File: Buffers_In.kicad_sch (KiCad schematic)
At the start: 29 parts, among them J1 NMJ6HCD2, U3 NE5532, U4 NE5532

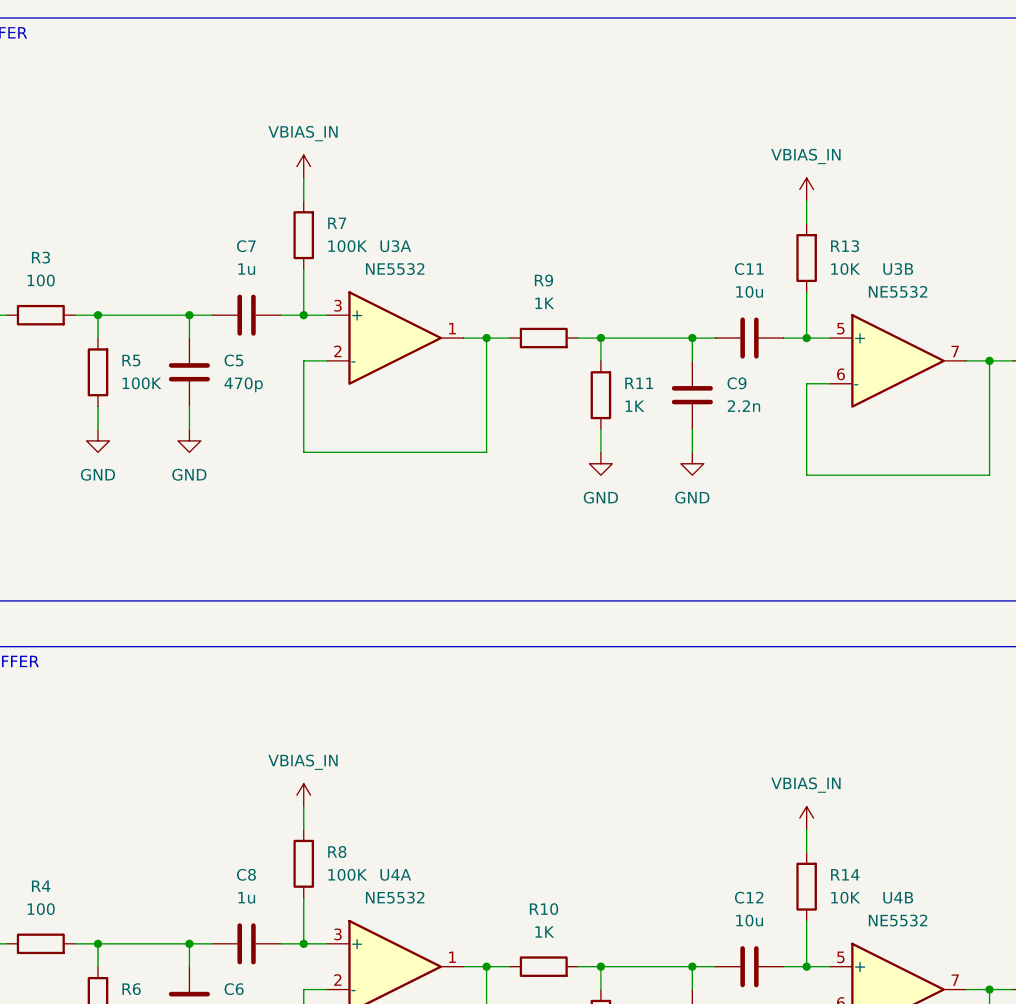
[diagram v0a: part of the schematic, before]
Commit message: Schematic
Updated the schematic.
Added the codec schematic module.
Added the buffer schematic module.
Added the RP2350 schematic module.
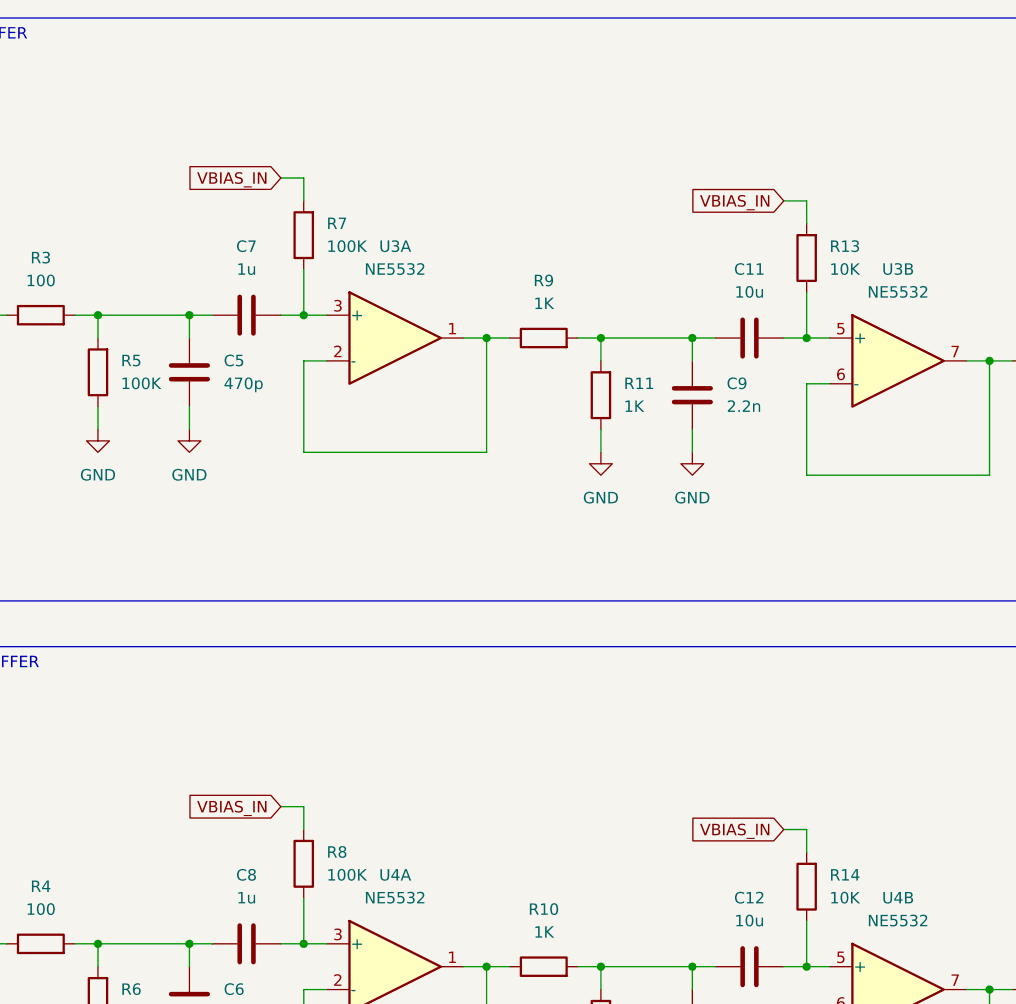
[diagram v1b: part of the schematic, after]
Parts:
- C10, C5, C6, C9: footprint (none) -> Capacitor_SMD:C_0603_1608Metric
- C11, C12, C13, C14: footprint (none) -> Capacitor_SMD:C_1206_3216Metric
- C7, C8: footprint (none) -> Capacitor_SMD:C_0805_2012Metric

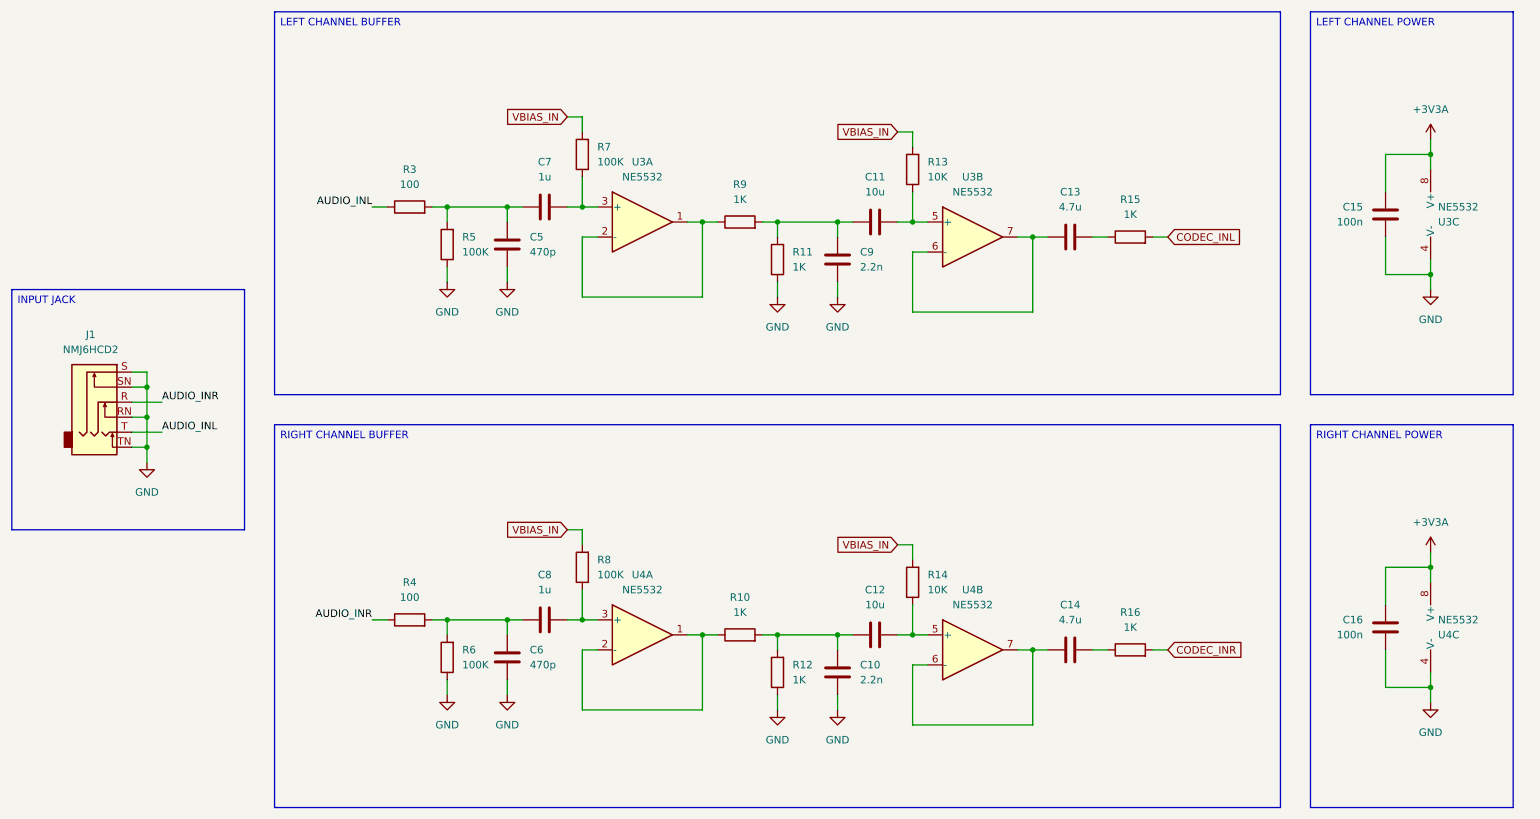
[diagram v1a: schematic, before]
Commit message: Schematic
Updated the power delivery module.
Other minor changes.
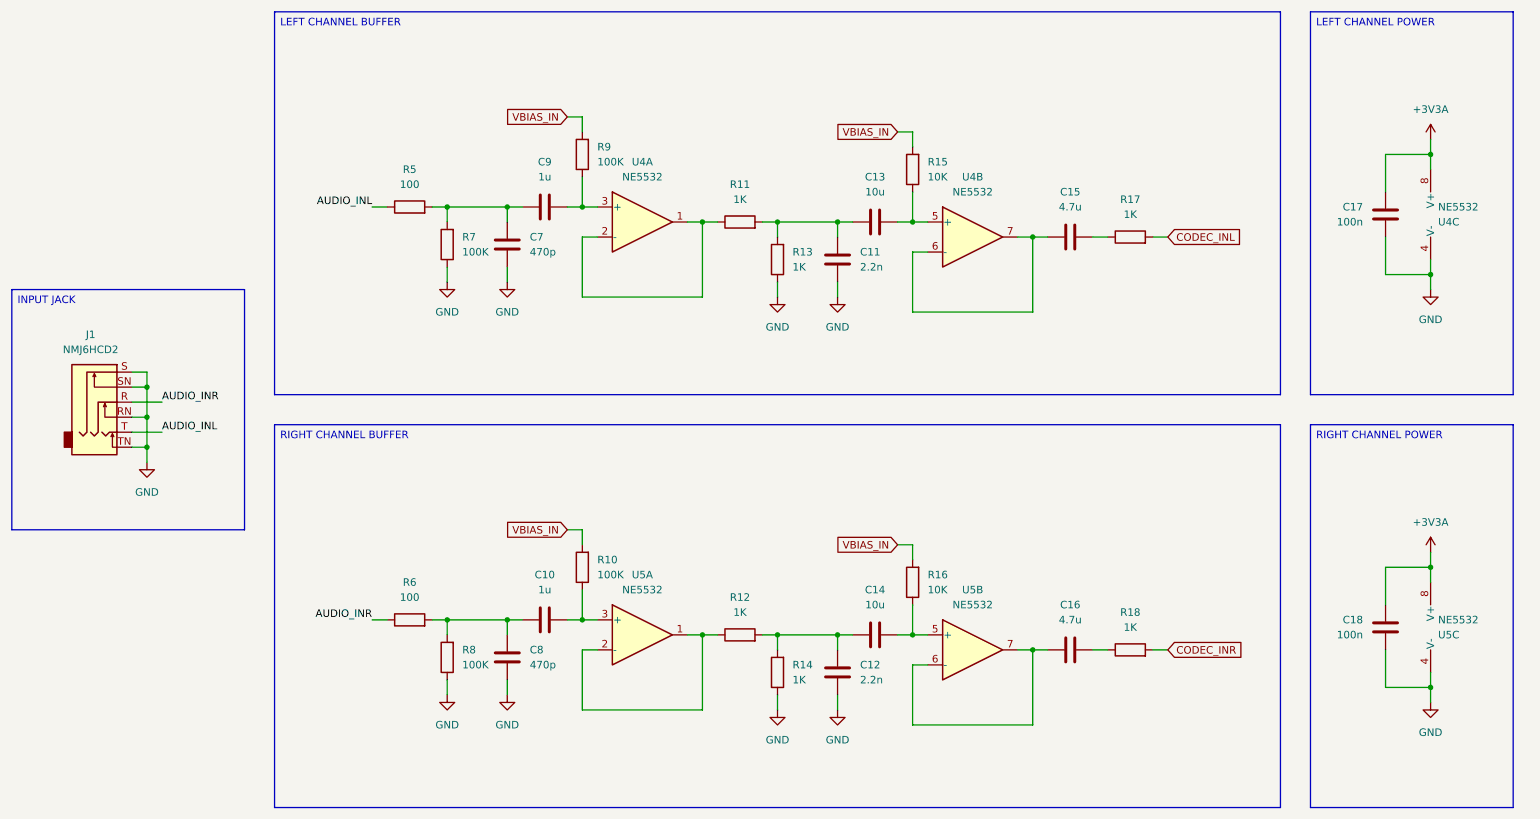
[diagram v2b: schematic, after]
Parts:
- renumbered C8 to C10, C9 to C11, C10 to C12, C11 to C13, C12 to C14, C13 to C15, C14 to C16, C15 to C17, C16 to C18, C5 to C7, C6 to C8, C7 to C9, R8 to R10, R9 to R11, R10 to R12, R11 to R13, R12 to R14, R13 to R15, R14 to R16, R15 to R17, R16 to R18, R3 to R5, R4 to R6, R5 to R7, R6 to R8, R7 to R9, U3 to U4, U4 to U5
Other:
- company: (none) -> DavidMolTor
- title: (none) -> SIMPLE CODEC

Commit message: Moved to a CS4272 codec as a cheaper alternative with similar performance.
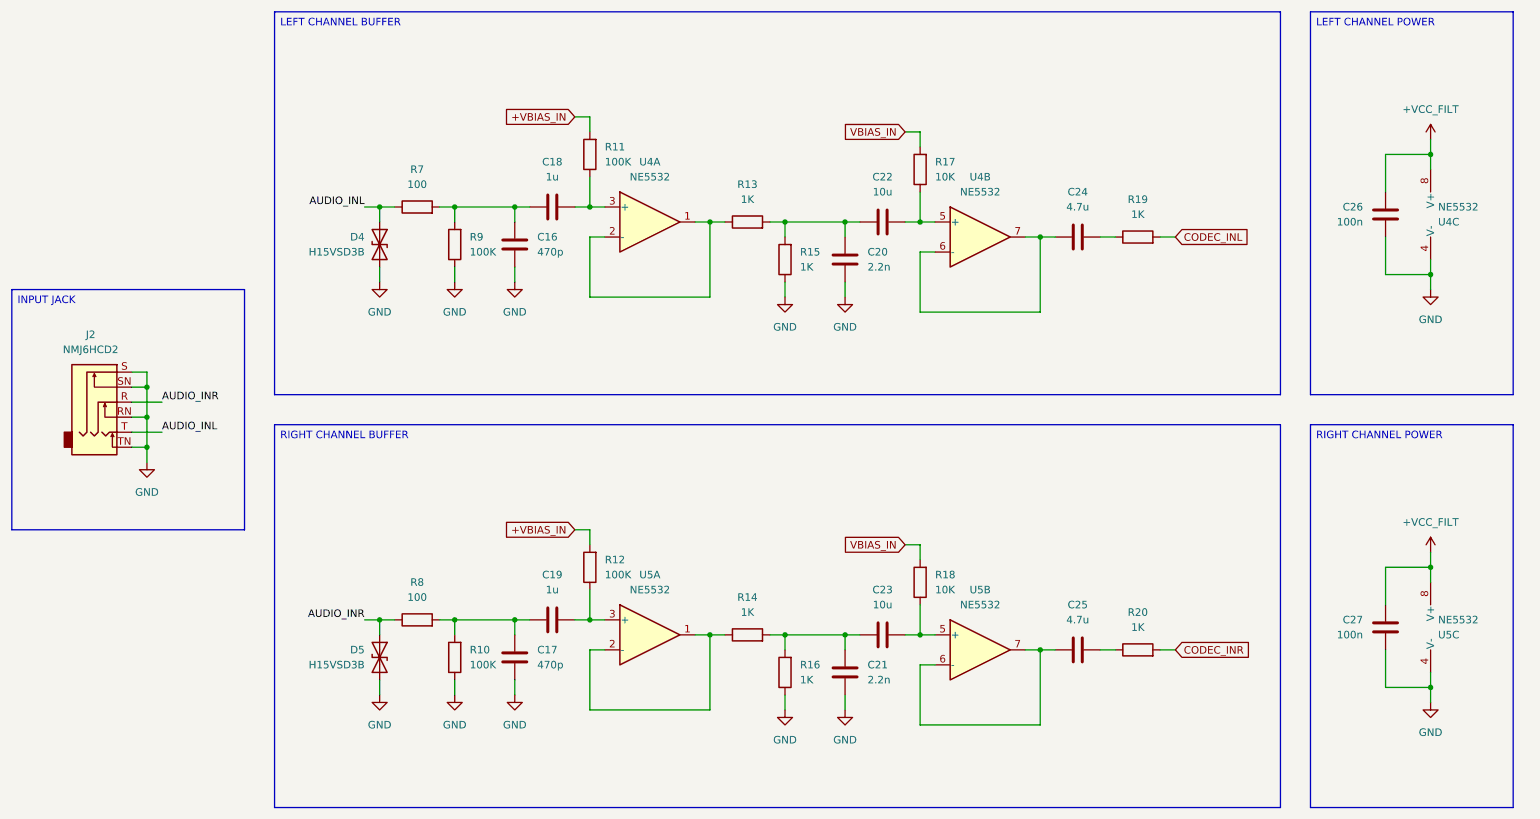
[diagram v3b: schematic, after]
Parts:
- added D4, D5: H15VSD3B, Diode_SMD:D_SOD-323, symbol Device:D_TVS
- renumbered C7 to C16, C8 to C17, C9 to C18, C10 to C19, C11 to C20, C12 to C21, C13 to C22, C14 to C23, C15 to C24, C16 to C25, C17 to C26, C18 to C27, J1 to J2, R8 to R10, R9 to R11, R10 to R12, R11 to R13, R12 to R14, R13 to R15, R14 to R16, R15 to R17, R16 to R18, R17 to R19, R18 to R20, R5 to R7, R6 to R8, R7 to R9
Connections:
- net AUDIO_INL: now also D4.1 (A1)
- net AUDIO_INR: now also D5.1 (A1)
- net GND: now also D4.2 (A2), D5.2 (A2)
- net VBIAS_IN: no longer R11.2, R12.2
- net +3V3A renamed +VCC_FILT
- new net +VBIAS_IN: R11.2, R12.2
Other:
- moved on the sheet: C16, C17, C18, C19, C20, C21, C22, C23, C24, C25, R10, R11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

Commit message: Initial layout
Initial layout inside a 1590N1/125B pedal enclosure.
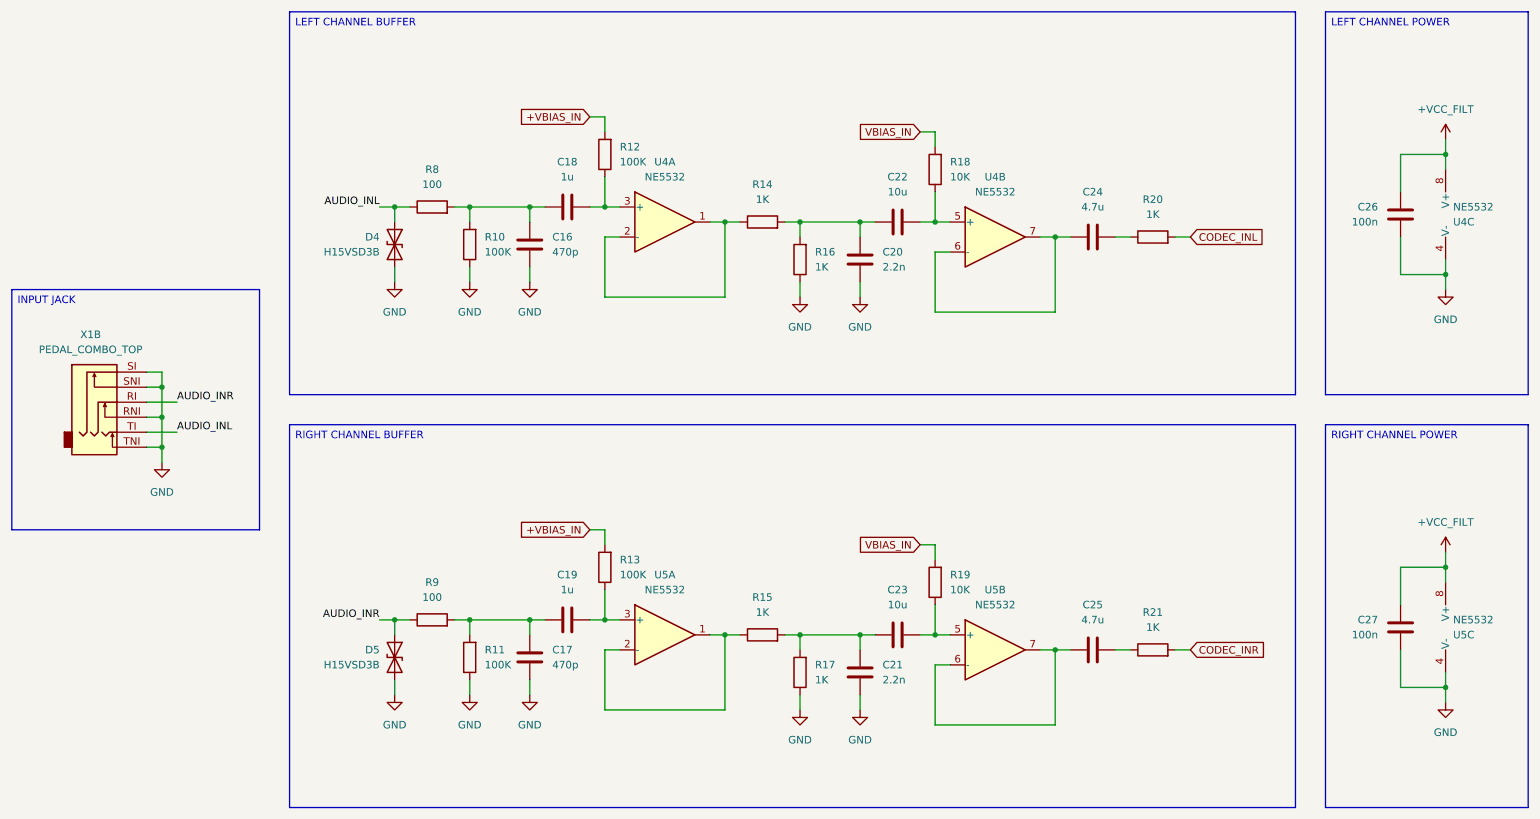
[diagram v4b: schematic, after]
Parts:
- removed J2: NMJ6HCD2, Custom_Parts:NMJ6HCD2_BORDER, symbol Connector_Audio:NMJ6HCD2
- added X1: PEDAL_COMBO_TOP, Custom_Parts:PEDAL_COMBO_TOP, symbol Custom_Parts:PEDAL_COMBO_TOP
- renumbered R9 to R10, R10 to R11, R11 to R12, R12 to R13, R13 to R14, R14 to R15, R15 to R16, R16 to R17, R17 to R18, R18 to R19, R19 to R20, R20 to R21, R7 to R8, R8 to R9
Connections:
- net AUDIO_INL: now also X1.TI
- net AUDIO_INR: now also X1.RI
- net GND: now also X1.RNI, X1.SI, X1.SNI, X1.TNI
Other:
- moved on the sheet: C16, C17, C18, C19, C20, C21, C22, C23, C24, C25, C26, C27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
